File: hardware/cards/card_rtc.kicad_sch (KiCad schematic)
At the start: 11 parts, among them U1 DS12C887, U2 74HCT138, U3 74HCT02, U4 74HCT08, U5 74HCT32, U6 74HCT04

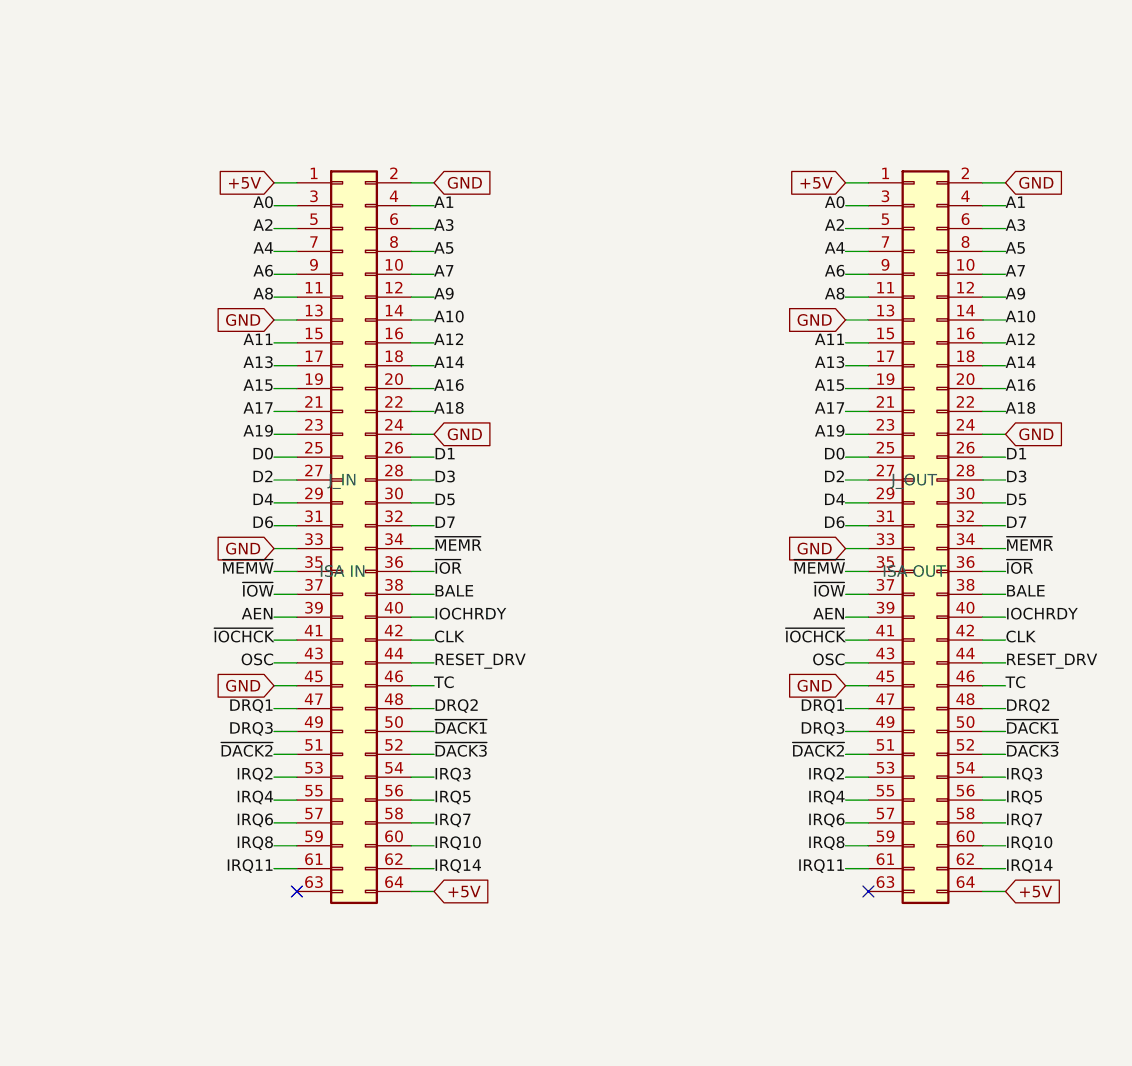
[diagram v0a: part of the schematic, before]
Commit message: Re-base ISA connector on standard 8-bit ISA pinout (60-pin, PicoGUS-style)
isa_conn now uses the standard 8-bit ISA edge pinout on a 60-pin 2.54mm header
(Conn_02x30_Odd_Even), matching the PicoGUS Bus_ISA_8bit layout so the sidecar and
dev cards are pin-compatible with real ISA cards (and 60-pin ribbon is easy to
source). The unused ISA analog rails are reclaimed: pin7 -5V->~{IOCHCK}, pin11
-12V->GND (extra return), pin15 +12V->IRQ8; pin13 reserved/0WS# left NC. Drops the
non-standard IRQ10/11/14 (16-bit-extension signals on a real AT); DACK0/REFRESH#
now on its standard pin (undriven, for card compatibility). Change is confined to
isa_conn.py; sidecar + all card_* sheets inherit it. Verified pin map and
connectivity (IOCHCK->Bus MCU, IRQ8->collector+RTC); zero structural ERC on
motherboard and all five cards.

Co-Authored-By: Claude Opus 4.8 (1M context) <noreply@anthropic.com>
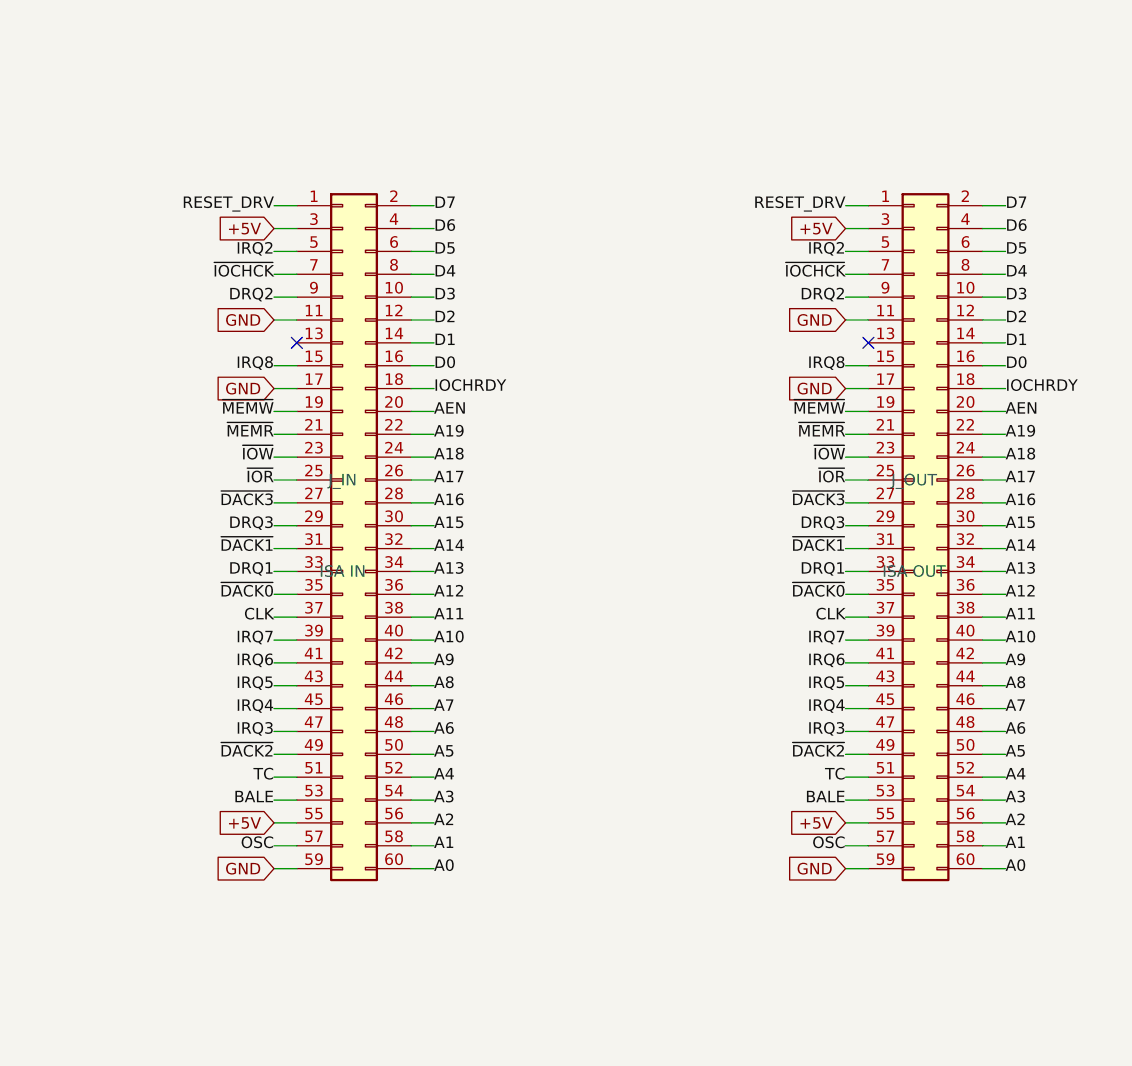
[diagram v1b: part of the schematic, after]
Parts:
- removed J_IN: ISA IN, symbol Connector_Generic:Conn_02x32_Odd_Even
- removed J_OUT: ISA OUT, symbol Connector_Generic:Conn_02x32_Odd_Even
- added J_IN: ISA IN, symbol Connector_Generic:Conn_02x30_Odd_Even
- added J_OUT: ISA OUT, symbol Connector_Generic:Conn_02x30_Odd_Even
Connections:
- net +5V: now also J_IN.3 (Pin_3), J_IN.55 (Pin_55), J_OUT.3 (Pin_3), J_OUT.55 (Pin_55)
- net A0: now also J_IN.60 (Pin_60), J_OUT.60 (Pin_60)
- net A1: now also J_IN.58 (Pin_58), J_OUT.58 (Pin_58)
- net A10: now also J_IN.40 (Pin_40), J_OUT.40 (Pin_40)
- net A11: now also J_IN.38 (Pin_38), J_OUT.38 (Pin_38)
- net A12: now also J_IN.36 (Pin_36), J_OUT.36 (Pin_36)
- net A13: now also J_IN.34 (Pin_34), J_OUT.34 (Pin_34)
- net A14: now also J_IN.32 (Pin_32), J_OUT.32 (Pin_32)
- net A15: now also J_IN.30 (Pin_30), J_OUT.30 (Pin_30)
- net A16: now also J_IN.28 (Pin_28), J_OUT.28 (Pin_28)
- net A17: now also J_IN.26 (Pin_26), J_OUT.26 (Pin_26)
- net A18: now also J_IN.24 (Pin_24), J_OUT.24 (Pin_24)
- net A19: now also J_IN.22 (Pin_22), J_OUT.22 (Pin_22)
- net A2: now also J_IN.56 (Pin_56), J_OUT.56 (Pin_56)
- net A3: now also J_IN.54 (Pin_54), J_OUT.54 (Pin_54)
- net A4: now also J_IN.52 (Pin_52), J_OUT.52 (Pin_52)
- net A5: now also J_IN.50 (Pin_50), J_OUT.50 (Pin_50)
- net A6: now also J_IN.48 (Pin_48), J_OUT.48 (Pin_48)
- net A7: now also J_IN.46 (Pin_46), J_OUT.46 (Pin_46)
- net A8: now also J_IN.44 (Pin_44), J_OUT.44 (Pin_44)
- net A9: now also J_IN.42 (Pin_42), J_OUT.42 (Pin_42)
- net AEN: now also J_IN.20 (Pin_20), J_OUT.20 (Pin_20)
- net BALE: now also J_IN.53 (Pin_53), J_OUT.53 (Pin_53)
- net CLK: now also J_IN.37 (Pin_37), J_OUT.37 (Pin_37)
- net D0: now also J_IN.16 (Pin_16), J_OUT.16 (Pin_16)
- net D1: now also J_IN.14 (Pin_14), J_OUT.14 (Pin_14)
- net D2: now also J_IN.12 (Pin_12), J_OUT.12 (Pin_12)
- net D3: now also J_IN.10 (Pin_10), J_OUT.10 (Pin_10)
- net D4: now also J_IN.8 (Pin_8), J_OUT.8 (Pin_8)
- net D5: now also J_IN.6 (Pin_6), J_OUT.6 (Pin_6)
- net D6: now also J_IN.4 (Pin_4), J_OUT.4 (Pin_4)
- net D7: now also J_IN.2 (Pin_2), J_OUT.2 (Pin_2)
- net DRQ1: now also J_IN.33 (Pin_33), J_OUT.33 (Pin_33)
- net DRQ2: now also J_IN.9 (Pin_9), J_OUT.9 (Pin_9)
- net DRQ3: now also J_IN.29 (Pin_29), J_OUT.29 (Pin_29)
- net GND: now also J_IN.11 (Pin_11), J_IN.17 (Pin_17), J_IN.59 (Pin_59), J_OUT.11 (Pin_11), J_OUT.17 (Pin_17), J_OUT.59 (Pin_59)
- net IOCHRDY: now also J_IN.18 (Pin_18), J_OUT.18 (Pin_18)
- net IRQ2: now also J_IN.5 (Pin_5), J_OUT.5 (Pin_5)
- net IRQ3: now also J_IN.47 (Pin_47), J_OUT.47 (Pin_47)
- net IRQ4: now also J_IN.45 (Pin_45), J_OUT.45 (Pin_45)
- net IRQ5: now also J_IN.43 (Pin_43), J_OUT.43 (Pin_43)
- net IRQ6: now also J_IN.41 (Pin_41), J_OUT.41 (Pin_41)
- net IRQ7: now also J_IN.39 (Pin_39), J_OUT.39 (Pin_39)
- net IRQ8: now also J_IN.15 (Pin_15), J_OUT.15 (Pin_15)
- net OSC: now also J_IN.57 (Pin_57), J_OUT.57 (Pin_57)
- net RESET_DRV: now also J_IN.1 (Pin_1), J_OUT.1 (Pin_1)
- net TC: now also J_IN.51 (Pin_51), J_OUT.51 (Pin_51)
- net ~{DACK1}: now also J_IN.31 (Pin_31), J_OUT.31 (Pin_31)
- net ~{DACK2}: now also J_IN.49 (Pin_49), J_OUT.49 (Pin_49)
- net ~{DACK3}: now also J_IN.27 (Pin_27), J_OUT.27 (Pin_27)
- net ~{IOCHCK}: now also J_IN.7 (Pin_7), J_OUT.7 (Pin_7)
- net ~{IOR}: now also J_IN.25 (Pin_25), J_OUT.25 (Pin_25)
- net ~{IOW}: now also J_IN.23 (Pin_23), J_OUT.23 (Pin_23)
- net ~{MEMR}: now also J_IN.21 (Pin_21), J_OUT.21 (Pin_21)
- net ~{MEMW}: now also J_IN.19 (Pin_19), J_OUT.19 (Pin_19)
- new net ~{DACK0}: J_IN.35 (Pin_35), J_OUT.35 (Pin_35)

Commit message: Drive ISA REFRESH# from the Bus MCU for DRAM-based cards
Pin 35 (DACK0/REFRESH#) net renamed ~{DACK0} -> ~{REFRESH} in isa_conn and is now
an active Bus MCU output (GPIO47, reclaimed from the redundant raw-~WR sense -- the
MCU tracks writes via the gated MEMW/IOW). Driven from the internal ~15us refresh
timer (same source as the 0x61-bit-4 toggle); a refresh cycle reuses the bus-master
engine to walk the row address on A0-A7 + pulse MEMR#, so DRAM ISA cards see a
standard refresh. ~{REFRESH} added to the Bus MCU interface. Verified it ties
sidecar<->Bus MCU and passes through J_IN<->J_OUT on every dev card; zero
structural ERC on motherboard and all five cards.

Co-Authored-By: Claude Opus 4.8 (1M context) <noreply@anthropic.com>
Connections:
- net ~{DACK0} renamed ~{REFRESH}
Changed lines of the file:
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@@
 		)
 	)
-	(label "~{DACK0}"
+	(label "~{REFRESH}"
 		(at 436.88 160.02 180)
 		(effects
@@
 		)
 	)
-	(label "~{DACK0}"
+	(label "~{REFRESH}"
 		(at 500.38 160.02 180)
 		(effects
@@
 		(instances
 			(project "card_rtc"
-				(path "/de7eed1a-e9a2-4107-9d35-860a76b8d710"
+				(path "/32d49c57-5828-4d7c-803d-106fd1e1bc19"
 					(reference "J_IN")
 					(unit 1)
@@
 		(instances
 			(project "card_rtc"
-				(path "/de7eed1a-e9a2-4107-9d35-860a76b8d710"
+				(path "/32d49c57-5828-4d7c-803d-106fd1e1bc19"
 					(reference "J_OUT")
 					(unit 1)
@@
 		(instances
 			(project "card_rtc"
-				(path "/de7eed1a-e9a2-4107-9d35-860a76b8d710"
+				(path "/32d49c57-5828-4d7c-803d-106fd1e1bc19"
 					(reference "U1")
 					(unit 1)
@@
 		(instances
 			(project "card_rtc"
-				(path "/de7eed1a-e9a2-4107-9d35-860a76b8d710"
+				(path "/32d49c57-5828-4d7c-803d-106fd1e1bc19"
 					(reference "R1")
 					(unit 1)
@@
 		(instances
 			(project "card_rtc"
-				(path "/de7eed1a-e9a2-4107-9d35-860a76b8d710"
+				(path "/32d49c57-5828-4d7c-803d-106fd1e1bc19"
 					(reference "U2")
 					(unit 1)
@@
 		(instances
 			(project "card_rtc"
-				(path "/de7eed1a-e9a2-4107-9d35-860a76b8d710"
+				(path "/32d49c57-5828-4d7c-803d-106fd1e1bc19"
 					(reference "U3")
 					(unit 1)
@@
 		(instances
 			(project "card_rtc"
-				(path "/de7eed1a-e9a2-4107-9d35-860a76b8d710"
+				(path "/32d49c57-5828-4d7c-803d-106fd1e1bc19"
 					(reference "U4")
 					(unit 1)
@@
 		(instances
 			(project "card_rtc"
-				(path "/de7eed1a-e9a2-4107-9d35-860a76b8d710"
+				(path "/32d49c57-5828-4d7c-803d-106fd1e1bc19"
 					(reference "U5")
 					(unit 1)
@@
 		(instances
 			(project "card_rtc"
-				(path "/de7eed1a-e9a2-4107-9d35-860a76b8d710"
+				(path "/32d49c57-5828-4d7c-803d-106fd1e1bc19"
 					(reference "U6")
 					(unit 1)
@@
 		(instances
 			(project "card_rtc"
-				(path "/de7eed1a-e9a2-4107-9d35-860a76b8d710"
+				(path "/32d49c57-5828-4d7c-803d-106fd1e1bc19"
 					(reference "C1")
 					(unit 1)
@@
 		(instances
 			(project "card_rtc"
-				(path "/de7eed1a-e9a2-4107-9d35-860a76b8d710"
+				(path "/32d49c57-5828-4d7c-803d-106fd1e1bc19"
 					(reference "C2")
 					(unit 1)

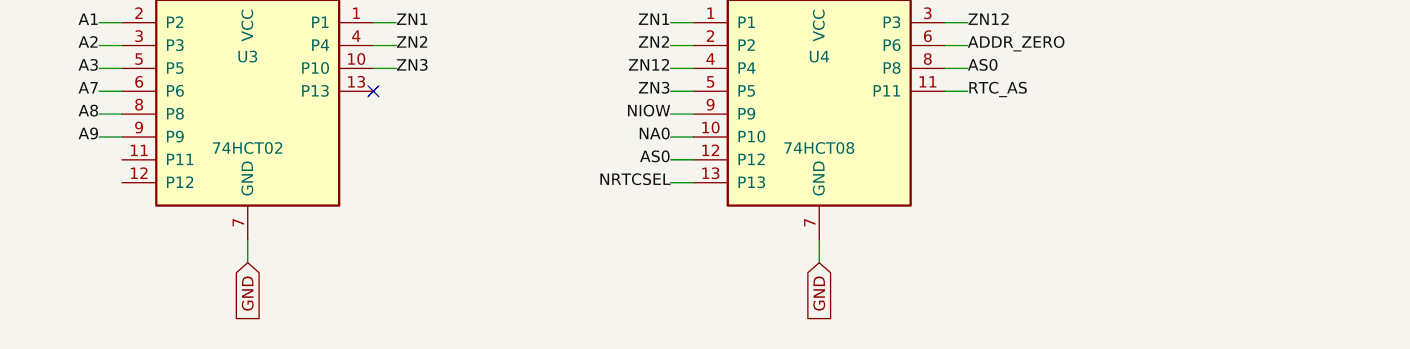
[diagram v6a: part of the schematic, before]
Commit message: Fix all low-severity + toolchain design-review findings
Low:
- LPT IRQ7 via tri-state '125 (NAND-enabled ack pulse) - shareable line
- card_com JP2 IRQ strap follows the base-address strap (was IRQ4-only)
- Supervisor USB-A VBUS fused (500mA polyfuse)
- card_isatest: DUT_PWR_EN moved to the control '595 (addr shifts can't
  glitch DUT power); '165s -> 74HC grade (HCT needs VCC 4.5-5.5V)
- /3 duty comments corrected; U13 marked load-bearing inverting buffer
- RTC AS hold-path bench note; duplicate ~RD stub removed
- mxbus PRIV_DECODE emptied (Y5 never leaves cpu_core)

Toolchain:
- build.py/build_cards return real exit codes, failing on structural ERC
  (endpoint_off_grid/unconnected_wire_endpoint/multiple_net_names) or a
  failed netlist export
- KiCad paths resolved via mxsch.kicad_cli()/kicad_symdir() (env, PATH,
  snap `current`) - no pinned snap revision anywhere
- Deterministic UUIDs (uuid5 title-seed + counter): rebuilds are
  byte-identical (verified); this rewrites every UUID once
- S-expression string escapes now round-trip (parse decodes, dump encodes)
- CLAUDE.md updated to match

The new structural gate immediately caught its own batch's bug (pull row
placed inside card_isatest's J2 pin field) - moved and re-verified.

Co-Authored-By: Claude Fable 5 <noreply@anthropic.com>
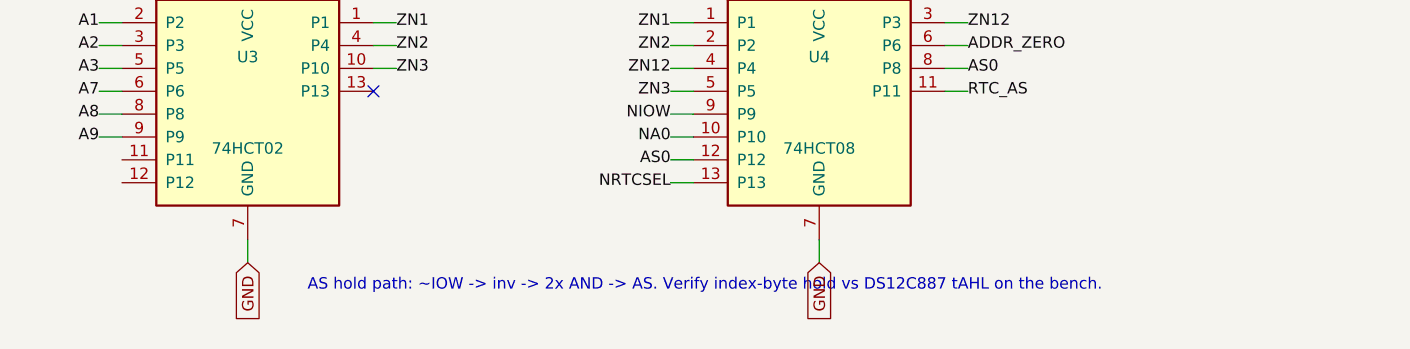
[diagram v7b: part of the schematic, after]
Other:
- note added: "AS hold path: ~IOW -> inv -> 2x AND -> AS. Verify index-byte hold vs DS12C887 tAHL on the bench."
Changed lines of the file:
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@@
+		)
+	)
+	(text "AS hold path: ~IOW -> inv -> 2x AND -> AS. Verify index-byte hold vs DS12C887 tAHL on the bench."
+		(at 139.7 236.22 0)
+		(effects
+			(font
+				(size 1.27 1.27)
+			)
 		)
 	)
@@
 		(instances
 			(project "card_rtc"
-				(path "/5ede661f-1489-40f7-b2df-eb1ebbd53da2"
+				(path "/8b82f227-8f3d-5d32-9aa5-3c6eb947efcb"
 					(reference "J_IN")
 					(unit 1)
@@
 		(instances
 			(project "card_rtc"
-				(path "/5ede661f-1489-40f7-b2df-eb1ebbd53da2"
+				(path "/8b82f227-8f3d-5d32-9aa5-3c6eb947efcb"
 					(reference "J_OUT")
 					(unit 1)
@@
 		(instances
 			(project "card_rtc"
-				(path "/5ede661f-1489-40f7-b2df-eb1ebbd53da2"
+				(path "/8b82f227-8f3d-5d32-9aa5-3c6eb947efcb"
 					(reference "U1")
 					(unit 1)
@@
 		(instances
 			(project "card_rtc"
-				(path "/5ede661f-1489-40f7-b2df-eb1ebbd53da2"
+				(path "/8b82f227-8f3d-5d32-9aa5-3c6eb947efcb"
 					(reference "R1")
 					(unit 1)
@@
 		(instances
 			(project "card_rtc"
-				(path "/5ede661f-1489-40f7-b2df-eb1ebbd53da2"
+				(path "/8b82f227-8f3d-5d32-9aa5-3c6eb947efcb"
 					(reference "U2")
 					(unit 1)
@@
 		(instances
 			(project "card_rtc"
-				(path "/5ede661f-1489-40f7-b2df-eb1ebbd53da2"
+				(path "/8b82f227-8f3d-5d32-9aa5-3c6eb947efcb"
 					(reference "U3")
 					(unit 1)
@@
 		(instances
 			(project "card_rtc"
-				(path "/5ede661f-1489-40f7-b2df-eb1ebbd53da2"
+				(path "/8b82f227-8f3d-5d32-9aa5-3c6eb947efcb"
 					(reference "U4")
 					(unit 1)
@@
 		(instances
 			(project "card_rtc"
-				(path "/5ede661f-1489-40f7-b2df-eb1ebbd53da2"
+				(path "/8b82f227-8f3d-5d32-9aa5-3c6eb947efcb"
 					(reference "U5")
 					(unit 1)
@@
 		(instances
 			(project "card_rtc"
-				(path "/5ede661f-1489-40f7-b2df-eb1ebbd53da2"
+				(path "/8b82f227-8f3d-5d32-9aa5-3c6eb947efcb"
 					(reference "U6")
 					(unit 1)
@@
 		(instances
 			(project "card_rtc"
-				(path "/5ede661f-1489-40f7-b2df-eb1ebbd53da2"
+				(path "/8b82f227-8f3d-5d32-9aa5-3c6eb947efcb"
 					(reference "C1")
 					(unit 1)
@@
 		(instances
 			(project "card_rtc"
-				(path "/5ede661f-1489-40f7-b2df-eb1ebbd53da2"
+				(path "/8b82f227-8f3d-5d32-9aa5-3c6eb947efcb"
 					(reference "C2")
 					(unit 1)

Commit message: JLCPCB sourcing pass: verify pinouts, LCSC part numbers, SMD build
Custom-symbol verification (open-questions Q5 resolved):
- MAX3241 symbol was wrong on nearly every pin and used MAX3243-style
  control names; regenerated to the real SSOP-28 pinout (SHDN#/EN#/
  R1OUTB/R2OUTB) and com_port rewired -- EN# must be GROUNDED (the old
  ~FORCEON-high would have disabled the receivers on real silicon)
- DS12C887 symbol wrong on 4 pins (DS=17, RESET#=18, IRQ#=19, SQW=23)

Sourcing (every part checked against the JLC DB; ~45 line items):
- New tools/parts.py maps (lib_id, value) -> LCSC; build.py applies it as
  an 'LCSC Part Num' property on every component (384 across the project)
- Sheets stay generic; stock-forced substitutions bound in the map:
  '374->'574 (parallel rewired), '163->'161, '157->HC157 (+HCT-buffered
  3.3V selects, I0/I1 swapped), '02->HC02, TCM809->MCP809, 2N3904->MMBT3904
- bus_mcu address counters moved to the 3.3V domain (HC161 on 3V3_BUS,
  loaded from MCU-side MD0-7; HCT244s read the 3.3V outputs at TTL Vih)
- 14.318 XOs are 3.3V-only parts: powered from 3V3, squared up via spare
  HCT gates (cpu_core U13, card_isatest U19)
- COM baud reference is now a 1.8432MHz crystal on the 16C550's XIN/XOUT
  (3.3V-only oscillators vs a 5V-only soft card)
- Supervisor QSPI header replaced with a real W25Q128JVSIQ
- Socket policy (fab installs sockets): V20 DIP-40, SRAM DIP-32 (no 5V
  512Kx8 SRAM at JLC at all), DS12C887 DIP-24, female headers for modules

Docs: CLAUDE.md fabrication-constraints section (SMD, 100x100mm, generic-
symbols rule, voltage-domain rule); README + hardware/README fab notes;
notes/jlcpcb-sourcing.md (decisions, thin-stock flags, not-at-JLC list);
stale questions-sidecar.md collapsed to its supersession record.

Rebuilt motherboard + cards: structural ERC 0, byte-identical rebuilds.

Co-Authored-By: Claude Fable 5 <noreply@anthropic.com>
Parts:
- C1, C2: LCSC Part Num (none) -> C14663
- J_IN, J_OUT: LCSC Part Num (none) -> C2333
- R1: LCSC Part Num (none) -> C25804
- U1: LCSC Part Num (none) -> C72120
- U2: LCSC Part Num (none) -> C5965
- U3: value 74HCT02 -> 74HC02; LCSC Part Num (none) -> C5588
- U4: LCSC Part Num (none) -> C5959
- U5: LCSC Part Num (none) -> C5985
- U6: LCSC Part Num (none) -> C672096
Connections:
- net RTC_DS: now also U1.17 (DS); no longer U1.16 (DS)
- net RTC_IRQ_L: now also U1.19 (~{IRQ}); no longer U1.18 (~{IRQ})
- net RTC_RST_L: now also U1.18 (~{RESET}); no longer U1.17 (~{RESET})
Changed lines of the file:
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@@
+			)
+		)
+		(property "LCSC Part Num" "C2333"
+			(at 444.5 152.4 0)
+			(effects
+				(font
+					(size 1.27 1.27)
+				)
+				(hide yes)
 			)
 		)
@@
 			)
 		)
+		(property "LCSC Part Num" "C2333"
+			(at 508 152.4 0)
+			(effects
+				(font
+					(size 1.27 1.27)
+				)
+				(hide yes)
+			)
+		)
 		(pin "1"
 		)
@@
 			)
 		)
+		(property "LCSC Part Num" "C72120"
+			(at 228.6 116.84 0)
+			(effects
+				(font
+					(size 1.27 1.27)
+				)
+				(hide yes)
+			)
+		)
 		(pin "4"
 		)
@@
 		(pin "14"
 		)
-		(pin "16"
+		(pin "17"
 		)
 		(pin "15"
@@
 		(pin "13"
 		)
-		(pin "17"
-		)
 		(pin "18"
 		)
-		(pin "21"
+		(pin "19"
+		)
+		(pin "23"
 		)
 		(pin "1"
@@
 			)
 		)
+		(property "LCSC Part Num" "C25804"
+			(at 254 88.9 0)
+			(effects
+				(font
+					(size 1.27 1.27)
+				)
+				(hide yes)
+			)
+		)
 		(pin "1"
 		)
@@
 			)
 		)
+		(property "LCSC Part Num" "C5965"
+			(at 88.9 81.28 0)
+			(effects
+				(font
+					(size 1.27 1.27)
+				)
+				(hide yes)
+			)
+		)
 		(pin "1"
 		)
@@
 			)
 		)
-		(property "Value" "74HCT02"
+		(property "Value" "74HC02"
 			(at 88.9 220.98 0)
 			(effects
@@
 		)
 		(property "Footprint" ""
+			(at 88.9 215.9 0)
+			(effects
+				(font
+					(size 1.27 1.27)
+				)
+				(hide yes)
+			)
+		)
+		(property "LCSC Part Num" "C5588"
 			(at 88.9 215.9 0)
 			(effects
@@
 			)
 		)
+		(property "LCSC Part Num" "C5959"
+			(at 152.4 215.9 0)
+			(effects
+				(font
+					(size 1.27 1.27)
+				)
+				(hide yes)
+			)
+		)
 		(pin "1"
 		)
@@
 			)
 		)
+		(property "LCSC Part Num" "C5985"
+			(at 152.4 160.02 0)
+			(effects
+				(font
+					(size 1.27 1.27)
+				)
+				(hide yes)
+			)
+		)
 		(pin "1"
 		)
@@
 			)
 		)
+		(property "LCSC Part Num" "C672096"
+			(at 88.9 160.02 0)
+			(effects
+				(font
+					(size 1.27 1.27)
+				)
+				(hide yes)
+			)
+		)
 		(pin "1"
 		)
@@
 			)
 		)
+		(property "LCSC Part Num" "C14663"
+			(at 228.6 175.26 0)
+			(effects
+				(font
+					(size 1.27 1.27)
+				)
+				(hide yes)
+			)
+		)
 		(pin "1"
 		)
@@
 			(at 152.4 96.52 0)
 			(effects
+				(font
+					(size 1.27 1.27)
+				)
+				(hide yes)
+			)
+		)
+		(property "LCSC Part Num" "C14663"
+			(at 152.4 96.52 0)
+			(effects
